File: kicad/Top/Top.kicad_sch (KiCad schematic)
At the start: 1 part

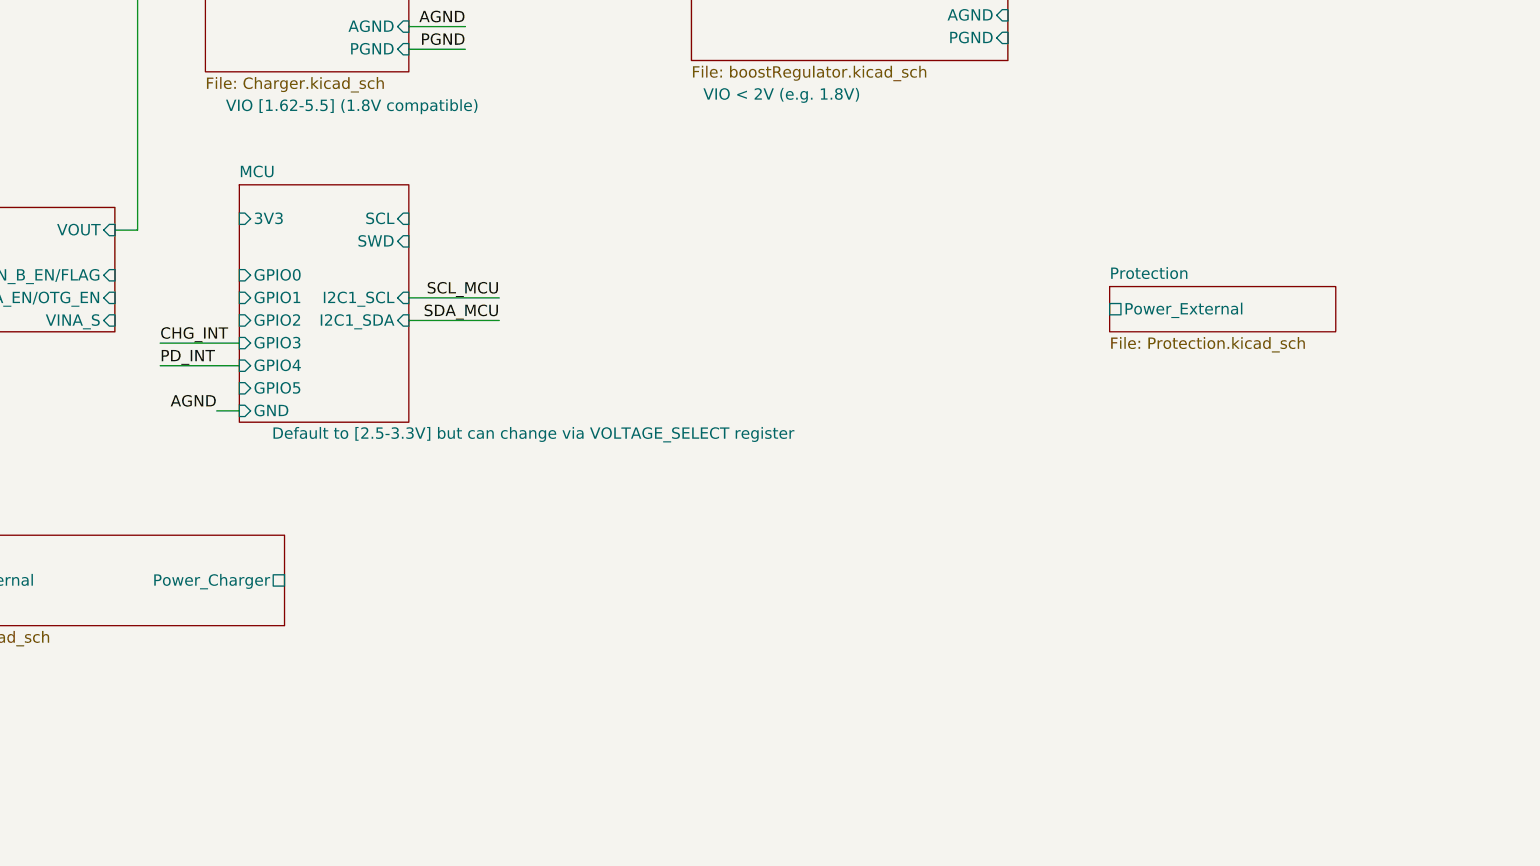
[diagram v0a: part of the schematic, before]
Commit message: Added overvoltage protection and filtering to ADC inputs of MCU
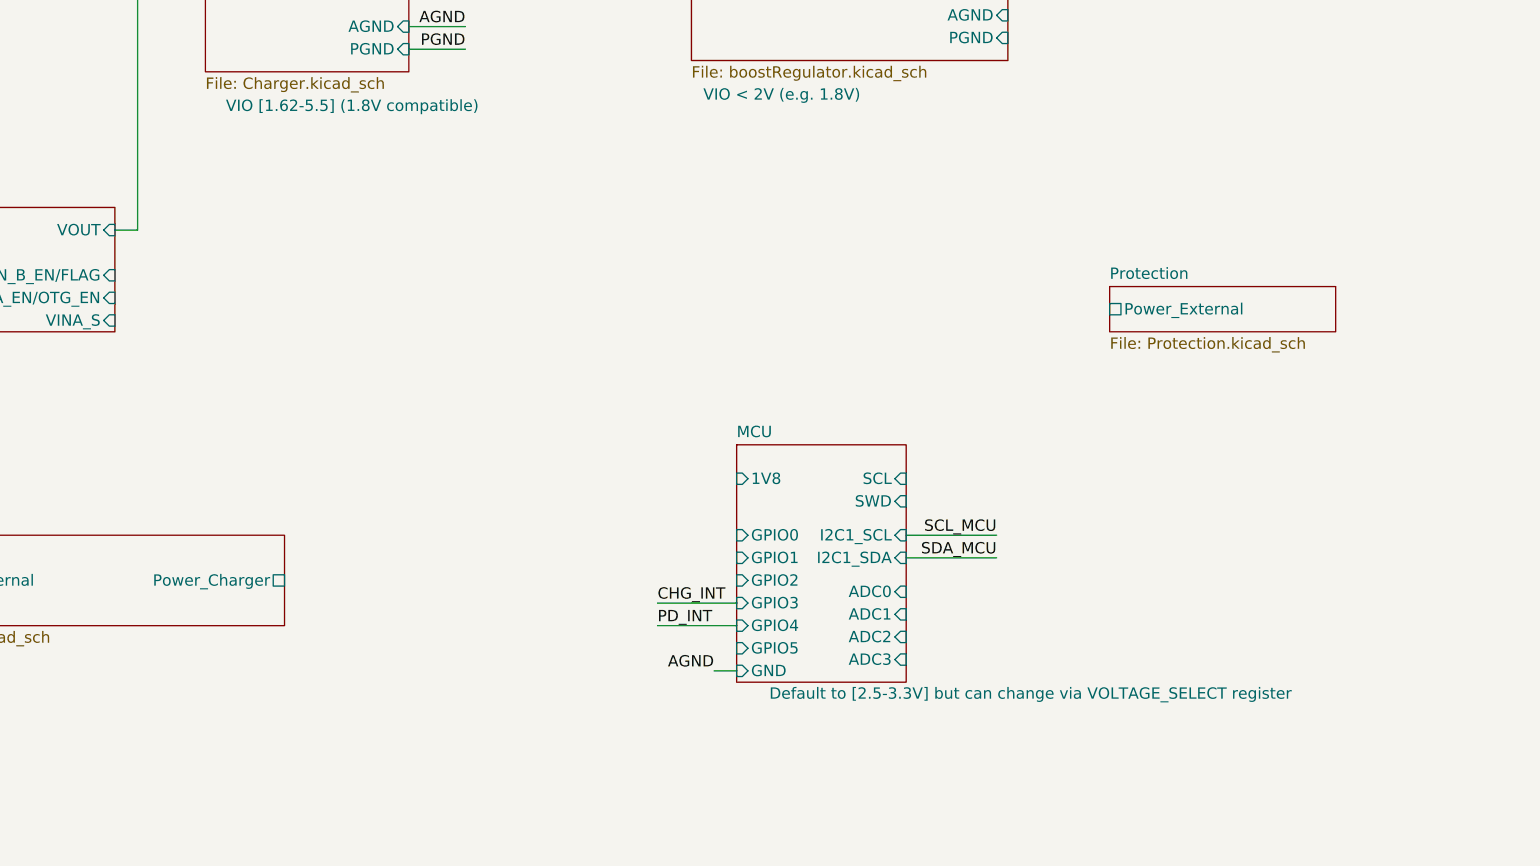
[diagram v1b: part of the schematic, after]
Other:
- sheet MCU ports: added 1V8, ADC0, ADC1, ADC2, ADC3; removed 3V3
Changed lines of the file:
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@@
     (stroke (width 0) (type default) (color 0 0 0 0))
   )
-  (wire (pts (xy 140.97 90.17) (xy 132.08 90.17))
+  (wire (pts (xy 196.85 119.38) (xy 187.96 119.38))
     (stroke (width 0) (type default) (color 0 0 0 0))
   )
@@
     (stroke (width 0) (type default) (color 0 0 0 0))
   )
-  (wire (pts (xy 138.43 97.79) (xy 140.97 97.79))
+  (wire (pts (xy 194.31 127) (xy 196.85 127))
     (stroke (width 0) (type default) (color 0 0 0 0))
   )
@@
     (stroke (width 0) (type default) (color 0 0 0 0))
   )
-  (wire (pts (xy 160.02 85.09) (xy 170.18 85.09))
+  (wire (pts (xy 215.9 111.76) (xy 226.06 111.76))
     (stroke (width 0) (type default) (color 0 0 0 0))
   )
@@
     (stroke (width 0) (type default) (color 0 0 0 0))
   )
-  (wire (pts (xy 160.02 87.63) (xy 170.18 87.63))
+  (wire (pts (xy 215.9 114.3) (xy 226.06 114.3))
     (stroke (width 0) (type default) (color 0 0 0 0))
   )
@@
     (stroke (width 0) (type default) (color 0 0 0 0))
   )
-  (wire (pts (xy 140.97 92.71) (xy 132.08 92.71))
+  (wire (pts (xy 196.85 121.92) (xy 187.96 121.92))
     (stroke (width 0) (type default) (color 0 0 0 0))
   )
@@
     (effects (font (size 1.27 1.27)) (justify left bottom))
   )
-  (label "CHG_INT" (at 132.08 90.17 0)
+  (label "CHG_INT" (at 187.96 119.38 0)
     (effects (font (size 1.27 1.27)) (justify left bottom))
   )
-  (label "AGND" (at 138.43 97.79 180)
+  (label "AGND" (at 194.31 127 180)
     (effects (font (size 1.27 1.27)) (justify right bottom))
   )
@@
     (effects (font (size 1.27 1.27)) (justify right bottom))
   )
-  (label "SCL_MCU" (at 170.18 85.09 180)
+  (label "SCL_MCU" (at 226.06 111.76 180)
     (effects (font (size 1.27 1.27)) (justify right bottom))
   )
@@
     (effects (font (size 1.27 1.27)) (justify right bottom))
   )
-  (label "SDA_MCU" (at 170.18 87.63 180)
+  (label "SDA_MCU" (at 226.06 114.3 180)
     (effects (font (size 1.27 1.27)) (justify right bottom))
   )
@@
     (effects (font (size 1.27 1.27)) (justify left bottom))
   )
-  (label "PD_INT" (at 132.08 92.71 0)
+  (label "PD_INT" (at 187.96 121.92 0)
     (effects (font (size 1.27 1.27)) (justify left bottom))
   )
@@
     )
   )
-  (sheet (at 140.97 72.39) (size 19.05 26.67)
+  (sheet (at 196.85 101.6) (size 19.05 26.67)
     (stroke (width 0.1524) (type solid) (color 0 0 0 0))
     (fill (color 0 0 0 0.0000))
-    (property "Sheet name" "MCU" (id 0) (at 140.97 71.6784 0)
+    (property "Sheet name" "MCU" (id 0) (at 196.85 100.8884 0)
       (effects (font (size 1.27 1.27)) (justify left bottom))
     )
-    (property "Sheet file" "mcu/RP2040_minimal/RP2040_minimal.kicad_sch" (id 1) (at 140.97 99.6446 0)
+    (property "Sheet file" "mcu/RP2040_minimal/RP2040_minimal.kicad_sch" (id 1) (at 196.85 128.8546 0)
       (effects (font (size 1.27 1.27)) (justify left top) hide)
     )
-    (property "VIO" "Default to [2.5-3.3V] but can change via VOLTAGE_SELECT register" (id 2) (at 173.99 100.33 0))
-    (pin "3V3" input (at 140.97 76.2 180)
-      (effects (font (size 1.27 1.27)) (justify left))
-    )
-    (pin "GND" input (at 140.97 97.79 180)
-      (effects (font (size 1.27 1.27)) (justify left))
-    )
-    (pin "SCL" input (at 160.02 76.2 0)
-      (effects (font (size 1.27 1.27)) (justify right))
-    )
-    (pin "SWD" input (at 160.02 78.74 0)
-      (effects (font (size 1.27 1.27)) (justify right))
-    )
-    (pin "GPIO0" input (at 140.97 82.55 180)
-      (effects (font (size 1.27 1.27)) (justify left))
-    )
-    (pin "GPIO1" input (at 140.97 85.09 180)
-      (effects (font (size 1.27 1.27)) (justify left))
-    )
-    (pin "GPIO2" input (at 140.97 87.63 180)
-      (effects (font (size 1.27 1.27)) (justify left))
-    )
-    (pin "GPIO4" input (at 140.97 92.71 180)
-      (effects (font (size 1.27 1.27)) (justify left))
-    )
-    (pin "GPIO5" input (at 140.97 95.25 180)
-      (effects (font (size 1.27 1.27)) (justify left))
-    )
-    (pin "GPIO3" input (at 140.97 90.17 180)
-      (effects (font (size 1.27 1.27)) (justify left))
-    )
-    (pin "I2C1_SDA" input (at 160.02 87.63 0)
-      (effects (font (size 1.27 1.27)) (justify right))
-    )
-    (pin "I2C1_SCL" input (at 160.02 85.09 0)
+    (property "VIO" "Default to [2.5-3.3V] but can change via VOLTAGE_SELECT register" (id 2) (at 229.87 129.54 0))
+    (pin "GND" input (at 196.85 127 180)
+      (effects (font (size 1.27 1.27)) (justify left))
+    )
+    (pin "SCL" input (at 215.9 105.41 0)
+      (effects (font (size 1.27 1.27)) (justify right))
+    )
+    (pin "SWD" input (at 215.9 107.95 0)
+      (effects (font (size 1.27 1.27)) (justify right))
+    )
+    (pin "GPIO0" input (at 196.85 111.76 180)
+      (effects (font (size 1.27 1.27)) (justify left))
+    )
+    (pin "GPIO1" input (at 196.85 114.3 180)
+      (effects (font (size 1.27 1.27)) (justify left))
+    )
+    (pin "GPIO2" input (at 196.85 116.84 180)
+      (effects (font (size 1.27 1.27)) (justify left))
+    )
+    (pin "GPIO4" input (at 196.85 121.92 180)
+      (effects (font (size 1.27 1.27)) (justify left))
+    )
+    (pin "GPIO5" input (at 196.85 124.46 180)
+      (effects (font (size 1.27 1.27)) (justify left))
+    )
+    (pin "GPIO3" input (at 196.85 119.38 180)
+      (effects (font (size 1.27 1.27)) (justify left))
+    )
+    (pin "I2C1_SDA" input (at 215.9 114.3 0)
+      (effects (font (size 1.27 1.27)) (justify right))
+    )
+    (pin "I2C1_SCL" input (at 215.9 111.76 0)
+      (effects (font (size 1.27 1.27)) (justify right))
+    )
+    (pin "1V8" input (at 196.85 105.41 180)
+      (effects (font (size 1.27 1.27)) (justify left))
+    )
+    (pin "ADC0" input (at 215.9 118.11 0)
+      (effects (font (size 1.27 1.27)) (justify right))
+    )
+    (pin "ADC1" input (at 215.9 120.65 0)
+      (effects (font (size 1.27 1.27)) (justify right))
+    )
+    (pin "ADC3" input (at 215.9 125.73 0)
+      (effects (font (size 1.27 1.27)) (justify right))
+    )
+    (pin "ADC2" input (at 215.9 123.19 0)
       (effects (font (size 1.27 1.27)) (justify right))
     )
@@
       (reference "C?") (unit 1) (value "0.1uF") (footprint "")
     )
+    (path "/b17a9dbb-4562-473a-b13f-bbad723355f8/4d39aff4-c202-44ad-ab7b-02c727dfb3a5"
+      (reference "C?") (unit 1) (value "0.22uF") (footprint "")
+    )
     (path "/3b7e5198-fb12-4059-9002-c176f652e784/4f212f16-2f95-4bc0-993a-9ebdc78c345f"
       (reference "C?") (unit 1) (value "10uF") (footprint "")
     )
+    (path "/b17a9dbb-4562-473a-b13f-bbad723355f8/51c69ac7-89fe-4936-afd1-8e1b54a62dc7"
+      (reference "C?") (unit 1) (value "0.22uF") (footprint "")
+    )
     (path "/427922e5-a943-4728-8788-709c0c3b2395/5c802776-019d-4191-be26-e60766a7622c"
       (reference "C?") (unit 1) (value "10uF") (footprint "")
@@
       (reference "C?") (unit 1) (value "100uF") (footprint "")
     )
+    (path "/b17a9dbb-4562-473a-b13f-bbad723355f8/7a8e481a-f817-4450-8309-0f45f2670710"
+      (reference "C?") (unit 1) (value "0.22uF") (footprint "")
+    )
     (path "/3fab603d-ed65-41bd-8de1-51639e39cb06/8c20b62f-b843-4bb9-80bb-6e0a3ea9e10b"
       (reference "C?") (unit 1) (value "27pF") (footprint "")
@@
       (reference "C?") (unit 1) (value "27pF") (footprint "")
     )
+    (path "/b17a9dbb-4562-473a-b13f-bbad723355f8/fd27b991-31b5-422b-8335-8ae8f4096cd6"
+      (reference "C?") (unit 1) (value "0.22uF") (footprint "")
+    )
     (path "/3fab603d-ed65-41bd-8de1-51639e39cb06/fe0d44e2-3fce-4edf-85f3-61612292df3d"
       (reference "C?") (unit 1) (value "1uF") (footprint "")
@@
       (reference "R65") (unit 1) (value "R_SEN") (footprint "AltiumImports:1206")
     )
+    (path "/b17a9dbb-4562-473a-b13f-bbad723355f8/19d6e89f-5af0-4248-ad27-14f3cf2d11c3"
+      (reference "R?") (unit 1) (value "1") (footprint "")
+    )
     (path "/3fab603d-ed65-41bd-8de1-51639e39cb06/1b80ca64-116f-4945-9b24-21286e6c3429"
       (reference "R?") (unit 1) (value "2.2k") (footprint "")
@@
       (reference "R?") (unit 1) (value "2.2k") (footprint "")
     )
+    (path "/b17a9dbb-4562-473a-b13f-bbad723355f8/5b015f8e-8625-4b26-abeb-7717424aa277"
+      (reference "R?") (unit 1) (value "1") (footprint "")
+    )
     (path "/3fab603d-ed65-41bd-8de1-51639e39cb06/67a27951-38d3-41ff-8bb4-03ba409ccf3b"
       (reference "R?") (unit 1) (value "24") (footprint "")
     )
+    (path "/b17a9dbb-4562-473a-b13f-bbad723355f8/8ed6ffed-c188-4c3d-9650-d6bdadbdf166"
+      (reference "R?") (unit 1) (value "1") (footprint "")
+    )
     (path "/3fab603d-ed65-41bd-8de1-51639e39cb06/94b378f8-4096-4e17-8960-317b21f96aaa"
       (reference "R?") (unit 1) (value "24") (footprint "")
@@
       (reference "R?") (unit 1) (value "649k") (footprint "")
     )
+    (path "/b17a9dbb-4562-473a-b13f-bbad723355f8/eee2cf32-834b-4256-8b49-b721c1b0b705"
+      (reference "R?") (unit 1) (value "1") (footprint "")
+    )
     (path "/427922e5-a943-4728-8788-709c0c3b2395/5348c353-2ef7-4ba8-ba47-d79055695ce1"
       (reference "SCL") (unit 1) (value "TestPoint") (footprint "")
@@
       (reference "U?") (unit 1) (value "MAX77857") (footprint "Package_BGA:WLP-35_7x5_2.828x2.028mm")
     )
+    (path "/b17a9dbb-4562-473a-b13f-bbad723355f8/242a1338-7bc6-4caa-952a-cdca6e10244e"
+      (reference "U?") (unit 1) (value "MCP6004T-I{slash}ST") (footprint "custom_amplifiers:MCP6004T-I&slash_ST")
+    )
     (path "/3b7e5198-fb12-4059-9002-c176f652e784/6a34cc5d-bb52-400f-93cd-0b434e28ff22"
